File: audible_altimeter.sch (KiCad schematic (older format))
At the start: 0 parts

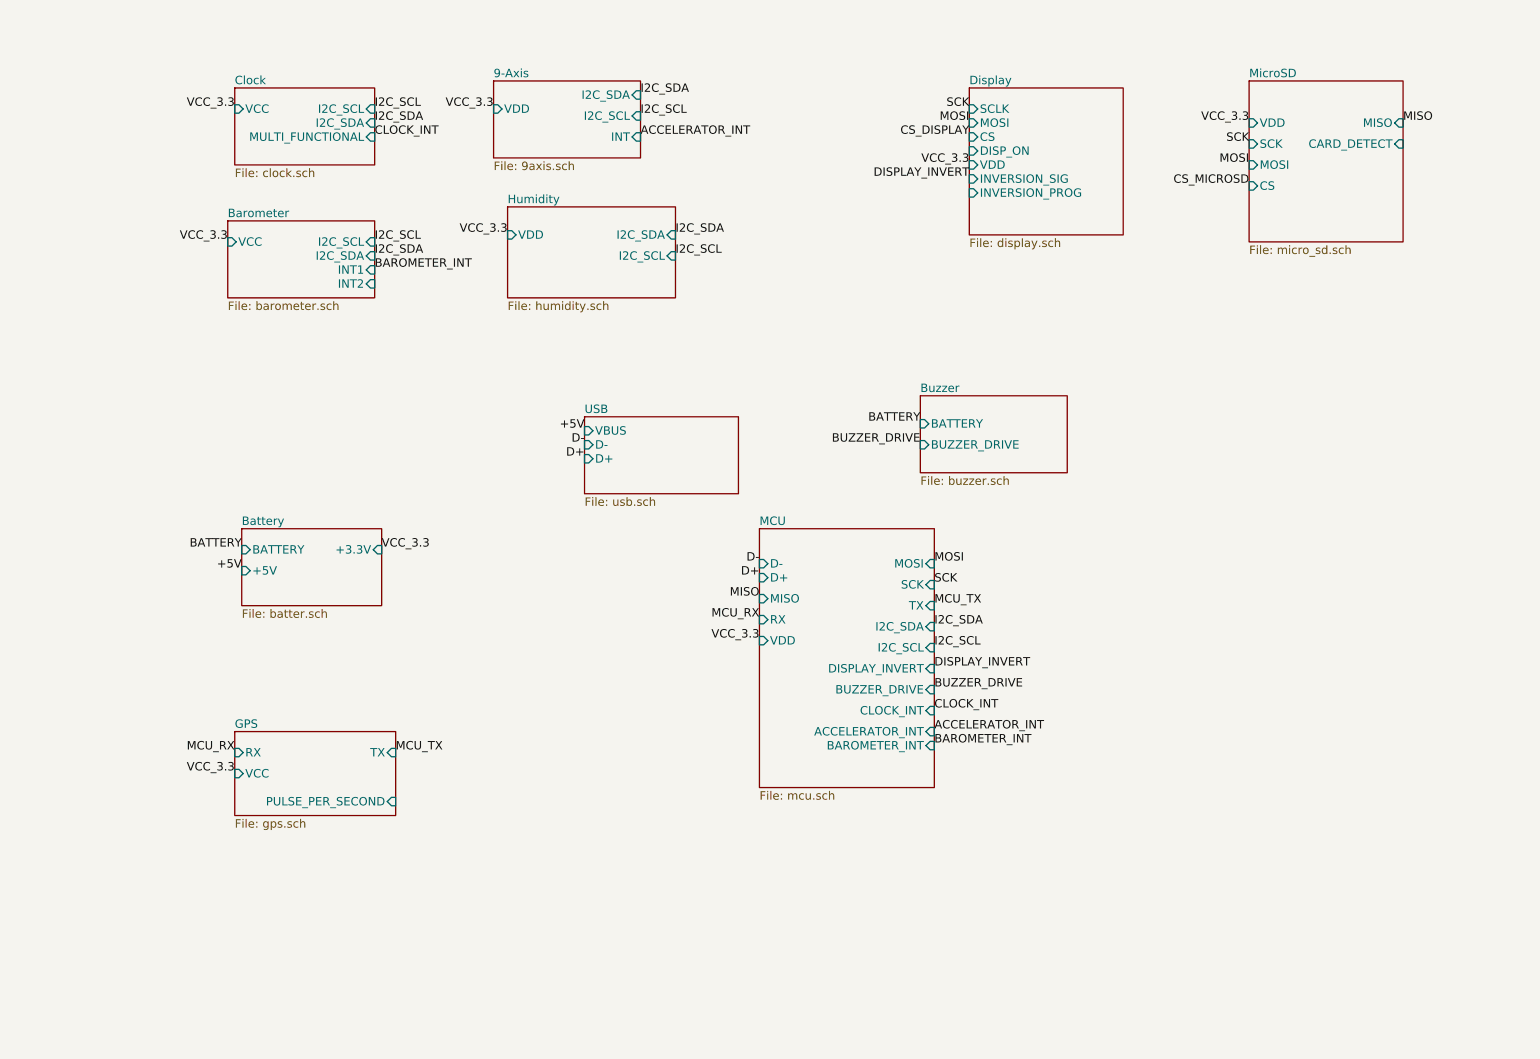
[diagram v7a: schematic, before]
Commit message: Add flash and ram. Some connections and DRC cleaning
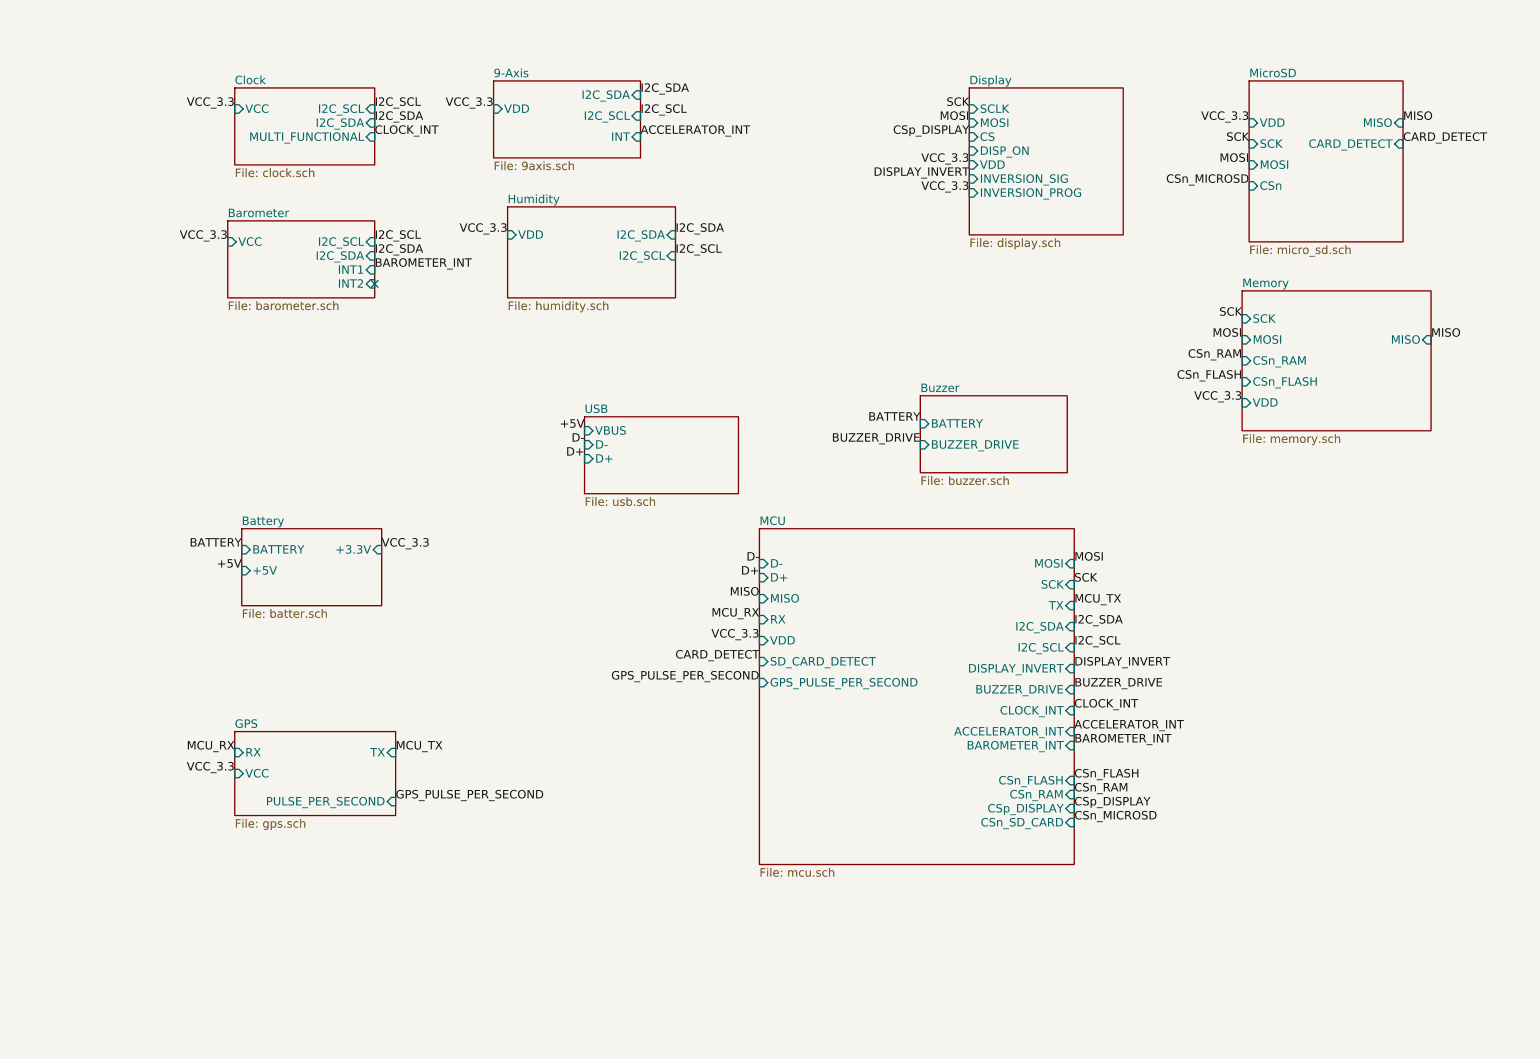
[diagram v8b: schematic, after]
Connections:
- no-connect marks 0 -> 1
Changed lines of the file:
@@
 $Descr A4 11693 8268
 encoding utf-8
-Sheet 1 12
+Sheet 1 13
 Title ""
 Date ""
@@
 F4 "MISO" I R 10700 1050 60
 F5 "MOSI" I L 9600 1350 60
-F6 "CS" I L 9600 1500 60
+F6 "CSn" I L 9600 1500 60
 F7 "CARD_DETECT" I R 10700 1200 60
 $EndSheet
@@
 $EndSheet
 $Sheet
-S 6100 3950 1250 1850
+S 6100 3950 2250 2400
 U 54464A80
 F0 "MCU" 60
@@
 F2 "D-" I L 6100 4200 60
 F3 "D+" I L 6100 4300 60
-F4 "MOSI" I R 7350 4200 60
+F4 "MOSI" I R 8350 4200 60
 F5 "MISO" I L 6100 4450 60
-F6 "SCK" I R 7350 4350 60
+F6 "SCK" I R 8350 4350 60
 F7 "RX" I L 6100 4600 60
-F8 "TX" I R 7350 4500 60
-F9 "I2C_SDA" I R 7350 4650 60
-F10 "I2C_SCL" I R 7350 4800 60
+F8 "TX" I R 8350 4500 60
+F9 "I2C_SDA" I R 8350 4650 60
+F10 "I2C_SCL" I R 8350 4800 60
 F11 "VDD" I L 6100 4750 60
-F12 "DISPLAY_INVERT" I R 7350 4950 60
-F13 "BUZZER_DRIVE" I R 7350 5100 60
-F14 "CLOCK_INT" I R 7350 5250 60
-F15 "ACCELERATOR_INT" I R 7350 5400 60
-F16 "BAROMETER_INT" I R 7350 5500 60
+F12 "DISPLAY_INVERT" I R 8350 4950 60
+F13 "BUZZER_DRIVE" I R 8350 5100 60
+F14 "CLOCK_INT" I R 8350 5250 60
+F15 "ACCELERATOR_INT" I R 8350 5400 60
+F16 "BAROMETER_INT" I R 8350 5500 60
+F17 "CSn_FLASH" I R 8350 5750 60
+F18 "CSn_RAM" I R 8350 5850 60
+F19 "CSp_DISPLAY" I R 8350 5950 60
+F20 "CSn_SD_CARD" I R 8350 6050 60
+F21 "SD_CARD_DETECT" I L 6100 4900 60
+F22 "GPS_PULSE_PER_SECOND" I L 6100 5050 60
 $EndSheet
 $Sheet
@@
 MOSI
 Text Label 9600 1500 2    60   ~ 0
-CS_MICROSD
+CSn_MICROSD
 Text Label 7600 1150 2    60   ~ 0
-CS_DISPLAY
+CSp_DISPLAY
 Text Label 7600 1050 2    60   ~ 0
 MOSI
 Text Label 10700 1050 0    60   ~ 0
 MISO
-Text Label 7350 4500 0    60   ~ 0
+Text Label 8350 4500 0    60   ~ 0
 MCU_TX
 Text Label 6100 4600 2    60   ~ 0
@@
 Text Label 2350 5700 2    60   ~ 0
 VCC_3.3
-Text Label 7350 4200 0    60   ~ 0
-MOSI
-Text Label 7350 4350 0    60   ~ 0
+Text Label 8350 4200 0    60   ~ 0
+MOSI
+Text Label 8350 4350 0    60   ~ 0
 SCK
 Text Label 6100 4450 2    60   ~ 0
@@
 Text Label 6100 4750 2    60   ~ 0
 VCC_3.3
-Text Label 7350 4800 0    60   ~ 0
-I2C_SCL
-Text Label 7350 4650 0    60   ~ 0
+Text Label 8350 4800 0    60   ~ 0
+I2C_SCL
+Text Label 8350 4650 0    60   ~ 0
 I2C_SDA
 Text Label 7250 3350 2    60   ~ 0
 BUZZER_DRIVE
-Text Label 7350 5100 0    60   ~ 0
+Text Label 8350 5100 0    60   ~ 0
 BUZZER_DRIVE
-Text Label 7350 4950 0    60   ~ 0
+Text Label 8350 4950 0    60   ~ 0
 DISPLAY_INVERT
 Text Label 7600 1450 2    60   ~ 0
 DISPLAY_INVERT
-Text Label 7350 5250 0    60   ~ 0
+Text Label 8350 5250 0    60   ~ 0
 CLOCK_INT
 Text Label 3350 1150 0    60   ~ 0
@@
 Text Label 3350 2100 0    60   ~ 0
 BAROMETER_INT
-Text Label 7350 5500 0    60   ~ 0
+Text Label 8350 5500 0    60   ~ 0
 BAROMETER_INT
-Text Label 7350 5400 0    60   ~ 0
+Text Label 8350 5400 0    60   ~ 0
 ACCELERATOR_INT
 Text Label 5250 1150 0    60   ~ 0
 ACCELERATOR_INT
+$Sheet
+S 9550 2250 1350 1000
+U 5462FBEF
+F0 "Memory" 60
+F1 "memory.sch" 60
+F2 "SCK" I L 9550 2450 60
+F3 "MOSI" I L 9550 2600 60
+F4 "MISO" I R 10900 2600 60
+F5 "CSn_RAM" I L 9550 2750 60
+F6 "CSn_FLASH" I L 9550 2900 60
+F7 "VDD" I L 9550 3050 60
+$EndSheet
+Text Label 9550 2450 2    60   ~ 0
+SCK
+Text Label 9550 2600 2    60   ~ 0
+MOSI
+Text Label 9550 2750 2    60   ~ 0
+CSn_RAM
+Text Label 9550 2900 2    60   ~ 0
+CSn_FLASH
+Text Label 9550 3050 2    60   ~ 0
+VCC_3.3
+Text Label 10900 2600 0    60   ~ 0
+MISO
+Text Label 8350 6050 0    60   ~ 0
+CSn_MICROSD
+Text Label 8350 5950 0    60   ~ 0
+CSp_DISPLAY
+Text Label 8350 5850 0    60   ~ 0
+CSn_RAM
+Text Label 8350 5750 0    60   ~ 0
+CSn_FLASH
+Text Label 10700 1200 0    60   ~ 0
+CARD_DETECT
+Text Label 6100 4900 2    60   ~ 0
+CARD_DETECT
+NoConn ~ 3350 2200
+Text Label 3500 5900 0    60   ~ 0
+GPS_PULSE_PER_SECOND
+Text Label 6100 5050 2    60   ~ 0
+GPS_PULSE_PER_SECOND
+Text Label 7600 1550 2    60   ~ 0
+VCC_3.3
 $EndSCHEMATC
